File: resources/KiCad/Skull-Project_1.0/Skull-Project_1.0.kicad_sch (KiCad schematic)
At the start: 8 parts, among them SW1 SW_SPST, SW2 SW_SPST

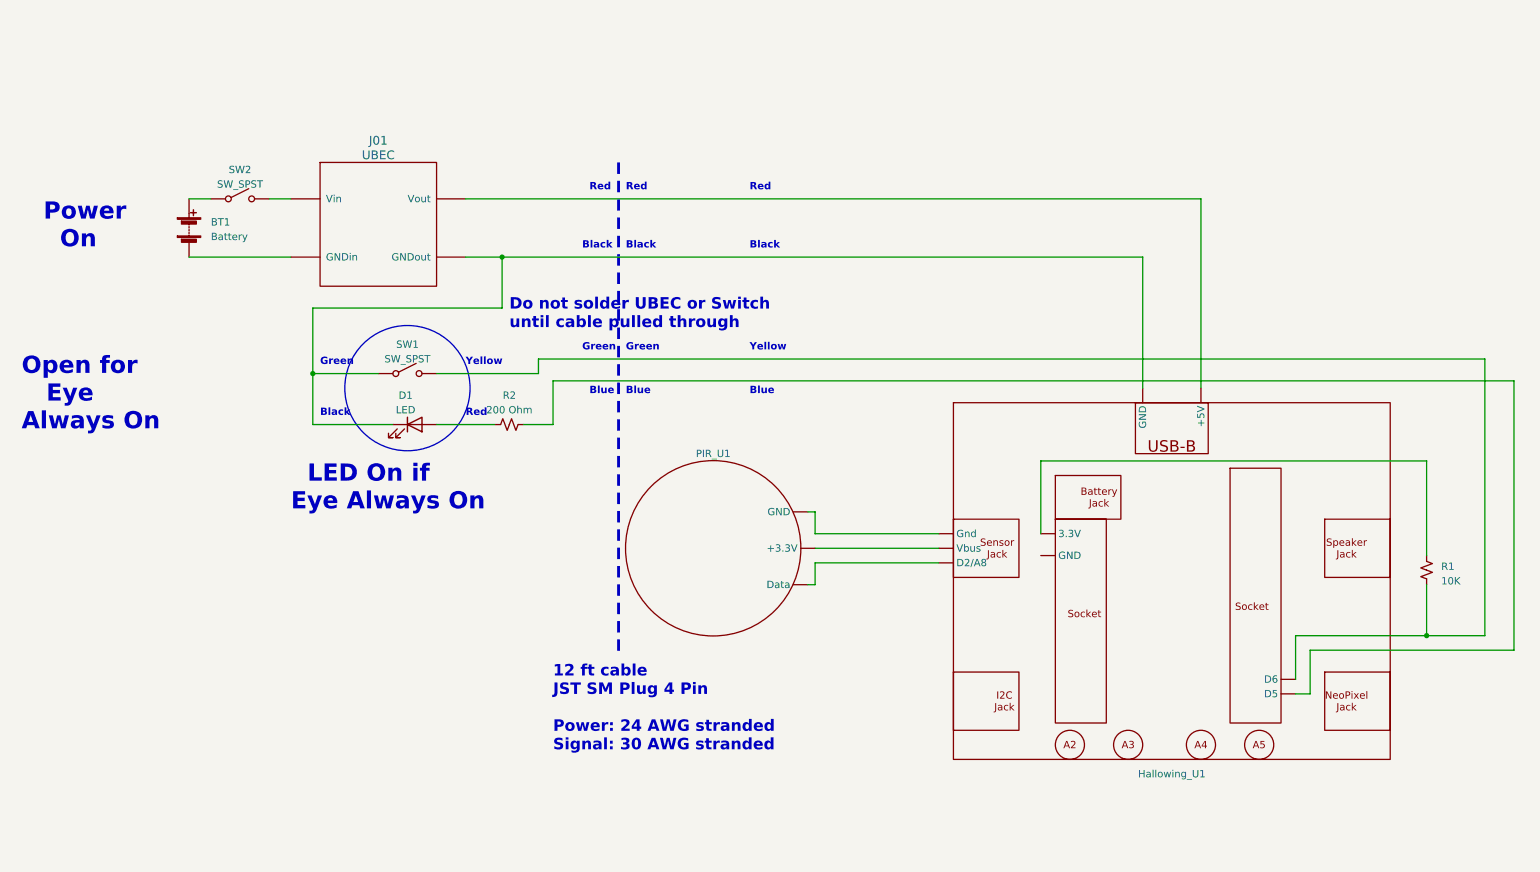
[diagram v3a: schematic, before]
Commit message: update schematic
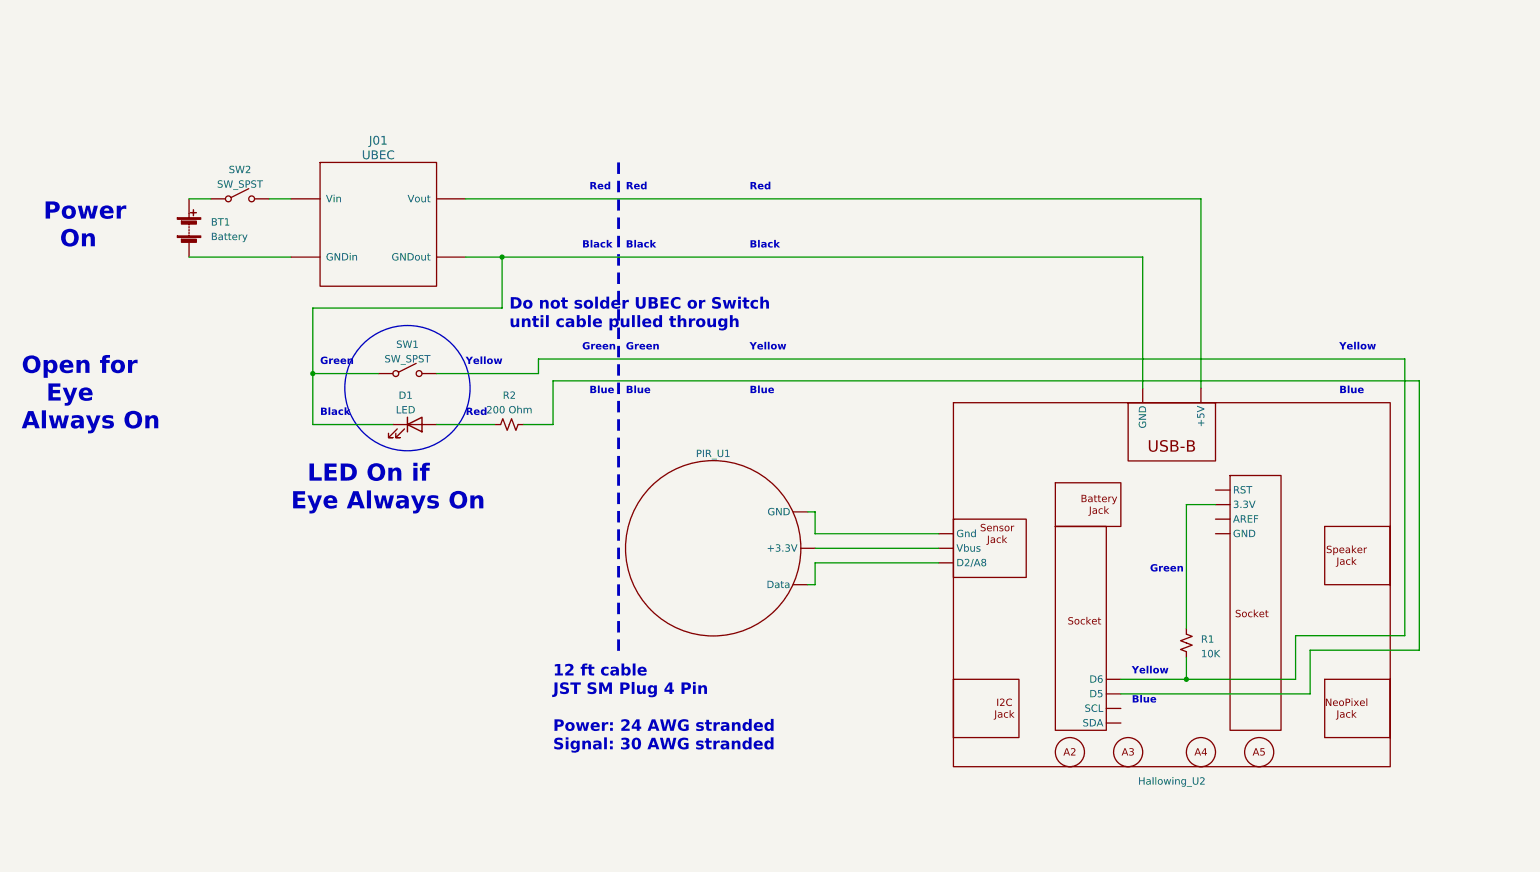
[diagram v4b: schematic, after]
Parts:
- removed Hallowing_U1: ~, symbol MDO:Hallowing_M4
- added Hallowing_U2: ~, symbol mdoLibrary:Hallowing_M4
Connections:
- net at R2.2: now also Hallowing_U2. (Vbus)
- net at R1.1: now also Hallowing_U2. (Vbus)
- net at R1.2, SW1.~ (B): now also Hallowing_U2. (Vbus)
- net at D1.1 (K), SW1.~ (B): now also Hallowing_U2. (Vbus)
- net at PIR_U1. (GND): now also Hallowing_U2. (Vbus)
- net at SW2.~ (B): now also BT1.1 (+)
- new net: Hallowing_U2. (Vbus), PIR_U1. (GND) (x2)
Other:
- moved on the sheet: R1
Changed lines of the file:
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@@
     (rev "1.0")
     (company "github.com/Mark-MDO47/Skull-Project")
-    (comment 1 "NOTE: Hallowing as from back (not display)")
+    (comment 1 "NOTE: Hallowing as from display side (not connector side)")
   )
   (junction (at 68.58 79.375) (diameter 0) (color 0 0 0 0)
@@
   (junction (at 101.6 59.055) (diameter 0) (color 0 0 0 0)
   )
-  (junction (at 262.89 125.095) (diameter 0) (color 0 0 0 0)
+  (junction (at 220.98 132.715) (diameter 0) (color 0 0 0 0)
   )
   (wire (pts (xy 100.33 88.265) (xy 90.17 88.265))
     (stroke (width 0) (type default))
   )
-  (wire (pts (xy 262.89 116.205) (xy 262.89 125.095))
-    (stroke (width 0) (type default))
-  )
-  (wire (pts (xy 242.57 135.255) (xy 242.57 127.635))
+  (wire (pts (xy 259.08 76.835) (xy 259.08 125.095))
+    (stroke (width 0) (type default))
+  )
+  (wire (pts (xy 220.98 128.905) (xy 220.98 132.715))
+    (stroke (width 0) (type default))
+  )
+  (wire (pts (xy 220.98 102.235) (xy 220.98 123.825))
+    (stroke (width 0) (type default))
+  )
+  (wire (pts (xy 223.52 48.895) (xy 223.52 81.915))
+    (stroke (width 0) (type default))
+  )
+  (wire (pts (xy 240.03 125.095) (xy 240.03 132.715))
     (stroke (width 0) (type default))
   )
@@
     (stroke (width 0) (type default))
   )
-  (wire (pts (xy 195.58 94.615) (xy 195.58 107.315))
-    (stroke (width 0) (type default))
-  )
-  (wire (pts (xy 278.13 127.635) (xy 278.13 80.645))
+  (wire (pts (xy 213.36 59.055) (xy 213.36 81.915))
     (stroke (width 0) (type default))
   )
@@
     (stroke (width 0) (type default))
   )
-  (wire (pts (xy 242.57 127.635) (xy 278.13 127.635))
+  (wire (pts (xy 242.57 127.635) (xy 261.62 127.635))
     (stroke (width 0) (type default))
   )
@@
     (stroke (width 0) (type default))
   )
-  (wire (pts (xy 240.03 125.095) (xy 240.03 132.715))
-    (stroke (width 0) (type default))
-  )
   (wire (pts (xy 156.21 103.505) (xy 156.21 107.315))
     (stroke (width 0) (type default))
   )
+  (wire (pts (xy 226.06 102.235) (xy 220.98 102.235))
+    (stroke (width 0) (type default))
+  )
   (wire (pts (xy 154.94 116.205) (xy 156.21 116.205))
     (stroke (width 0) (type default))
   )
-  (wire (pts (xy 240.03 125.095) (xy 262.89 125.095))
-    (stroke (width 0) (type default))
-  )
-  (wire (pts (xy 213.36 59.055) (xy 213.36 81.915))
-    (stroke (width 0) (type default))
-  )
-  (wire (pts (xy 223.52 48.895) (xy 223.52 81.915))
+  (wire (pts (xy 242.57 135.255) (xy 209.55 135.255))
     (stroke (width 0) (type default))
   )
@@
     (stroke (width 0) (type default))
   )
-  (wire (pts (xy 273.05 125.095) (xy 262.89 125.095))
+  (wire (pts (xy 240.03 125.095) (xy 259.08 125.095))
     (stroke (width 0) (type default))
   )
@@
     (stroke (width 0) (type default))
   )
+  (wire (pts (xy 242.57 127.635) (xy 242.57 135.255))
+    (stroke (width 0) (type default))
+  )
   (wire (pts (xy 101.6 59.055) (xy 213.36 59.055))
     (stroke (width 0) (type default))
@@
     (stroke (width 0) (type default))
   )
-  (wire (pts (xy 195.58 94.615) (xy 262.89 94.615))
-    (stroke (width 0) (type default))
-  )
-  (wire (pts (xy 240.03 135.255) (xy 242.57 135.255))
-    (stroke (width 0) (type default))
-  )
-  (wire (pts (xy 262.89 94.615) (xy 262.89 111.125))
-    (stroke (width 0) (type default))
-  )
-  (wire (pts (xy 273.05 76.835) (xy 273.05 125.095))
+  (wire (pts (xy 259.08 76.835) (xy 107.95 76.835))
+    (stroke (width 0) (type default))
+  )
+  (wire (pts (xy 209.55 132.715) (xy 220.98 132.715))
     (stroke (width 0) (type default))
   )
@@
     (stroke (width 0) (type default))
   )
+  (wire (pts (xy 261.62 80.645) (xy 261.62 127.635))
+    (stroke (width 0) (type default))
+  )
   (wire (pts (xy 60.96 48.895) (xy 64.77 48.895))
     (stroke (width 0) (type default))
   )
-  (wire (pts (xy 278.13 80.645) (xy 110.49 80.645))
+  (wire (pts (xy 220.98 132.715) (xy 240.03 132.715))
     (stroke (width 0) (type default))
   )
@@
     (stroke (width 0) (type default))
   )
-  (wire (pts (xy 273.05 76.835) (xy 107.95 76.835))
-    (stroke (width 0) (type default))
-  )
   (wire (pts (xy 46.99 59.055) (xy 64.77 59.055))
     (stroke (width 0) (type default))
@@
     (stroke (width 0) (type default))
   )
+  (wire (pts (xy 261.62 80.645) (xy 110.49 80.645))
+    (stroke (width 0) (type default))
+  )
   (circle (center 85.09 81.915) (radius 10.925)
     (stroke (width 0) (type default))
@@
   (text "Blue" (at 116.84 83.185 0)
     (effects (font (size 1.27 1.27) bold) (justify left bottom))
+  )
+  (text "Blue" (at 247.65 83.185 0)
+    (effects (font (size 1.27 1.27) bold) (justify left bottom))
+  )
+  (text "Green" (at 214.63 114.3 0)
+    (effects (font (size 1.27 1.27) (thickness 0.254) bold) (justify left bottom))
   )
   (text "Red" (at 95.25 86.995 0)
@@
     (effects (font (size 3 3) (thickness 0.6) bold) (justify left bottom))
   )
+  (text "Yellow" (at 247.65 75.565 0)
+    (effects (font (size 1.27 1.27) bold) (justify left bottom))
+  )
   (text "Green" (at 123.19 75.565 0)
     (effects (font (size 1.27 1.27) (thickness 0.254) bold) (justify left bottom))
@@
   (text "Green" (at 115.57 75.565 0)
     (effects (font (size 1.27 1.27) (thickness 0.254) bold) (justify left bottom))
+  )
+  (text "Yellow" (at 211.455 132.08 0)
+    (effects (font (size 1.27 1.27) bold) (justify left bottom))
   )
   (text "12 ft cable\nJST SM Plug 4 Pin\n\nPower: 24 AWG stranded\nSignal: 30 AWG stranded"
@@
     (effects (font (size 1.27 1.27) bold) (justify left bottom))
   )
-  (symbol (lib_id "MDO:Hallowing_M4") (at 218.44 83.185 0) (unit 1)
-    (in_bom yes) (on_board yes) (dnp no) (fields_autoplaced)
-    (property "Reference" "Hallowing_U1" (at 218.44 149.225 0)
-      (effects (font (size 1.27 1.27)))
-    )
-    (property "Value" "~" (at 218.44 83.185 0)
-      (effects (font (size 1.27 1.27)))
-    )
-    (property "Footprint" "" (at 218.44 83.185 0)
-      (effects (font (size 1.27 1.27)) hide)
-    )
-    (property "Datasheet" "" (at 218.44 83.185 0)
-      (effects (font (size 1.27 1.27)) hide)
-    )
-    (pin "")
-    (pin "")
-    (pin "")
-    (pin "")
-    (pin "")
-    (pin "")
-    (pin "")
-    (pin "")
-    (pin "")
-    (instances
-      (project "Skull-Project_1.0"
-        (path "/13d7b3b4-5d80-4b2f-98bb-c8334b3eaf59"
-          (reference "Hallowing_U1") (unit 1)
-        )
-      )
-    )
+  (text "Blue" (at 211.455 137.16 0)
+    (effects (font (size 1.27 1.27) bold) (justify left bottom))
   )
   (symbol (lib_id "MDO:UBEC") (at 77.47 55.245 0) (unit 1)
@@
     )
   )
-  (symbol (lib_id "Device:R_Small_US") (at 262.89 113.665 0) (unit 1)
-    (in_bom yes) (on_board yes) (dnp no) (fields_autoplaced)
-    (property "Reference" "R1" (at 265.43 113.03 0)
+  (symbol (lib_id "mdoLibrary:Hallowing_M4") (at 218.44 84.455 0) (unit 1)
+    (in_bom yes) (on_board yes) (dnp no) (fields_autoplaced)
+    (property "Reference" "Hallowing_U2" (at 218.44 150.495 0)
+      (effects (font (size 1.27 1.27)))
+    )
+    (property "Value" "~" (at 218.44 84.455 0)
+      (effects (font (size 1.27 1.27)))
+    )
+    (property "Footprint" "" (at 218.44 84.455 0)
+      (effects (font (size 1.27 1.27)) hide)
+    )
+    (property "Datasheet" "" (at 218.44 84.455 0)
+      (effects (font (size 1.27 1.27)) hide)
+    )
+    (pin "")
+    (pin "")
+    (pin "")
+    (pin "")
+    (pin "")
+    (pin "")
+    (pin "")
+    (pin "")
+    (pin "")
+    (pin "")
+    (pin "")
+    (pin "")
+    (pin "")
+    (instances
+      (project "Skull-Project_1.0"
+        (path "/13d7b3b4-5d80-4b2f-98bb-c8334b3eaf59"
+          (reference "Hallowing_U2") (unit 1)
+        )
+      )
+    )
+  )
+  (symbol (lib_id "Device:R_Small_US") (at 220.98 126.365 0) (unit 1)
+    (in_bom yes) (on_board yes) (dnp no) (fields_autoplaced)
+    (property "Reference" "R1" (at 223.52 125.73 0)
       (effects (font (size 1.27 1.27)) (justify left))
     )
-    (property "Value" "10K" (at 265.43 115.57 0)
+    (property "Value" "10K" (at 223.52 128.27 0)
       (effects (font (size 1.27 1.27)) (justify left))
     )
-    (property "Footprint" "" (at 262.89 113.665 0)
-      (effects (font (size 1.27 1.27)) hide)
-    )
-    (property "Datasheet" "~" (at 262.89 113.665 0)
-      (effects (font (size 1.27 1.27)) hide)
-    )
+    (property "Footprint" "" (at 220.98 126.365 0)
+      (effects (font (size 1.27 1.27)) hide)
+    )
+    (property "Datasheet" "~" (at 220.98 126.365 0)
+      (effects (font (size 1.27 1.27)) hide)
+    )

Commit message: add optional 2nd eye
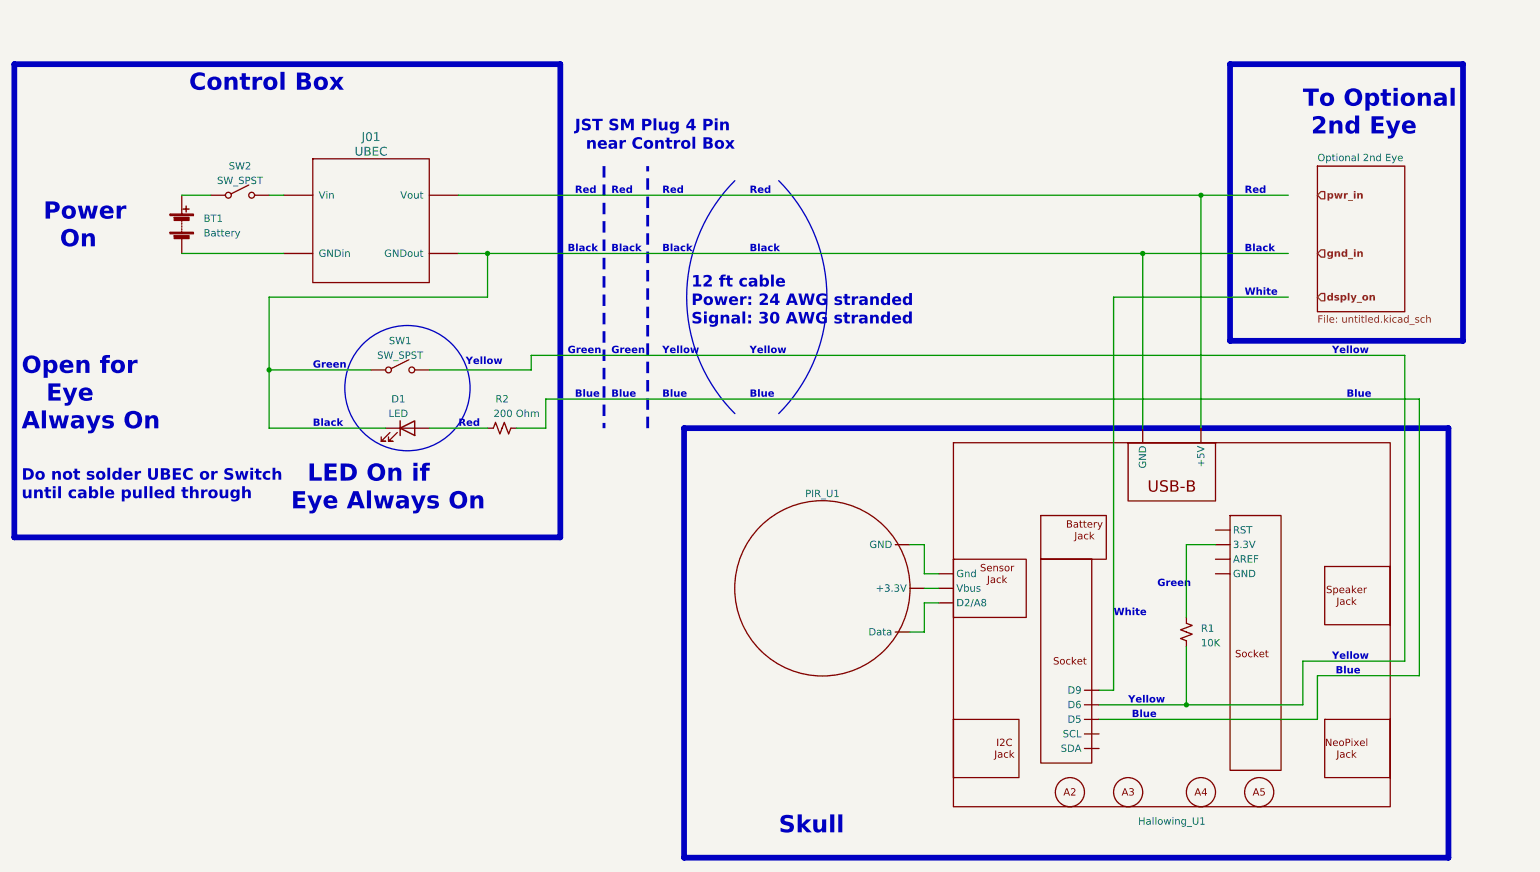
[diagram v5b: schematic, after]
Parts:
- removed Hallowing_U2: ~, symbol mdoLibrary:Hallowing_M4
- added Hallowing_U1: ~, symbol mdoLibrary:Hallowing_M4
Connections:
- net at R2.2: now also Hallowing_U1. (Vbus)
- net at SW2.~ (B): now also BT1.1 (+)
- net at R1.1: now also Hallowing_U1. (Vbus)
- net at R1.2, SW1.~ (B): now also Hallowing_U1. (Vbus)
- net at D1.1 (K), SW1.~ (B): now also Hallowing_U1. (Vbus)
- net at PIR_U1. (GND): now also Hallowing_U1. (Vbus)
- new net: Hallowing_U1. (Vbus), PIR_U1. (GND) (x2)
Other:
- added sheet Optional 2nd Eye (untitled.kicad_sch)
- note added: "12 ft cable Power: 24 AWG stranded Signal: 30 AWG stranded"
- note added: "Control Box"
- note added: "JST SM Plug 4 Pin near Control Box"
- note added: "Skull"
- note added: "To Optional 2nd Eye"
- note added: "White"
- note removed: "12 ft cable JST SM Plug 4 Pin Power: 24 AWG stranded Signal: 30 AWG stranded"
- moved on the sheet: BT1, D1, R1, R2, SW1, SW2

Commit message: add Microwave Sensor for option two eyes
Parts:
- removed PIR_U1: ~, symbol MDO:PIR
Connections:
- net GND: now reaches Hallowing_U1. (Vbus)
- net at SW2.~ (B): now also BT1.1 (+)
- new net: Hallowing_U1. (Vbus), R1.2, SW1.~ (B)
- new net 5V: Hallowing_U1. (Vbus)
- new net Data: Hallowing_U1. (Vbus)
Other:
- added sheet Peson Sensor (PersonSensor.kicad_sch)
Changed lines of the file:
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@@
     (stroke (width 0) (type default))
   )
-  (wire (pts (xy 172.72 109.22) (xy 175.26 109.22))
+  (wire (pts (xy 160.02 109.22) (xy 175.26 109.22))
     (stroke (width 0) (type default))
   )
@@
     (stroke (width 0) (type default))
   )
-  (wire (pts (xy 172.72 124.46) (xy 175.26 124.46))
+  (wire (pts (xy 160.02 124.46) (xy 175.26 124.46))
     (stroke (width 0) (type default))
   )
@@
     (stroke (width 0) (type default))
   )
-  (wire (pts (xy 175.26 116.84) (xy 177.8 116.84))
+  (wire (pts (xy 160.02 116.84) (xy 177.8 116.84))
     (stroke (width 0) (type default))
   )
@@
     (effects (font (size 1.27 1.27) bold) (justify left bottom))
   )
+  (hierarchical_label "GND" (shape input) (at 160.02 109.22 180) (fields_autoplaced)
+    (effects (font (size 2 2)) (justify right))
+  )
+  (hierarchical_label "RST" (shape input) (at 160.02 132.08 180) (fields_autoplaced)
+    (effects (font (size 2 2)) (justify right))
+  )
   (hierarchical_label "pwr_in" (shape input) (at 243.84 48.26 0) (fields_autoplaced)
     (effects (font (size 1.27 1.27) bold) (justify left))
   )
+  (hierarchical_label "5V" (shape input) (at 160.02 116.84 180) (fields_autoplaced)
+    (effects (font (size 2 2)) (justify right))
+  )
   (hierarchical_label "dsply_on" (shape input) (at 243.84 66.04 0) (fields_autoplaced)
     (effects (font (size 1.27 1.27) bold) (justify left))
+  )
+  (hierarchical_label "Data" (shape input) (at 160.02 124.46 180) (fields_autoplaced)
+    (effects (font (size 2 2)) (justify right))
   )
   (hierarchical_label "gnd_in" (shape input) (at 243.84 58.42 0) (fields_autoplaced)
@@
         (path "/13d7b3b4-5d80-4b2f-98bb-c8334b3eaf59"
           (reference "J01") (unit 1)
-        )
-      )
-    )
-  )
-  (symbol (lib_name "PIR_1") (lib_id "MDO:PIR") (at 157.48 137.16 0) (unit 1)
-    (in_bom yes) (on_board yes) (dnp no) (fields_autoplaced)
-    (property "Reference" "PIR_U1" (at 157.48 100.33 0)
-      (effects (font (size 1.27 1.27)))
-    )
-    (property "Value" "~" (at 157.48 137.16 0)
-      (effects (font (size 1.27 1.27)))
-    )
-    (property "Footprint" "" (at 157.48 137.16 0)
-      (effects (font (size 1.27 1.27)) hide)
-    )
-    (property "Datasheet" "" (at 157.48 137.16 0)
-      (effects (font (size 1.27 1.27)) hide)
-    )
-    (pin "")
-    (pin "")
-    (pin "")
-    (instances
-      (project "Skull-Project_1.0"
-        (path "/13d7b3b4-5d80-4b2f-98bb-c8334b3eaf59"
-          (reference "PIR_U1") (unit 1)
         )
       )
@@
       )
     )
+  )
+  (sheet (at 144.78 103.505) (size 12.7 36.195) (fields_autoplaced)
+    (stroke (width 0.1524) (type solid))
+    (fill (color 0 0 0 0.0000))
+    (property "Sheetname" "Peson Sensor" (at 144.78 102.7934 0)
+      (effects (font (size 1.27 1.27)) (justify left bottom))
+    )
+    (property "Sheetfile" "PersonSensor.kicad_sch" (at 144.78 140.2846 0)
+      (effects (font (size 1.27 1.27)) (justify left top))
+    )
+    (property "Field2" "" (at 144.78 103.505 0)
+      (effects (font (size 1.27 1.27)) hide)
+    )
+    (instances
+      (project "Skull-Project_1.0"
+        (path "/13d7b3b4-5d80-4b2f-98bb-c8334b3eaf59" (page "3"))
+      )
+    )
